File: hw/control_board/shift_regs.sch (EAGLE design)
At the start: 137 parts, among them IC1 74HC595D, IC13 STM32F10XCXT6, IC2 74HC595D, IC3 74HC595D, IC4 74HC595D, IC5 74HC595D, IC6 74HC595D, IC7 74HC595D, IC8 74HC595D, IC9 ESP8266, Q1 4MHz, Q2 32768KHz, T1 BC847, T10 BC847, T11 BC847, T12 BC847, T13 BC847, T14 BC847, T15 BC847, T16 BC847, T2 BC847, T3 BC847, T4 BC847, T5 BC847, T6 BC847, T7 BC847, T8 BC847, T9 BC847

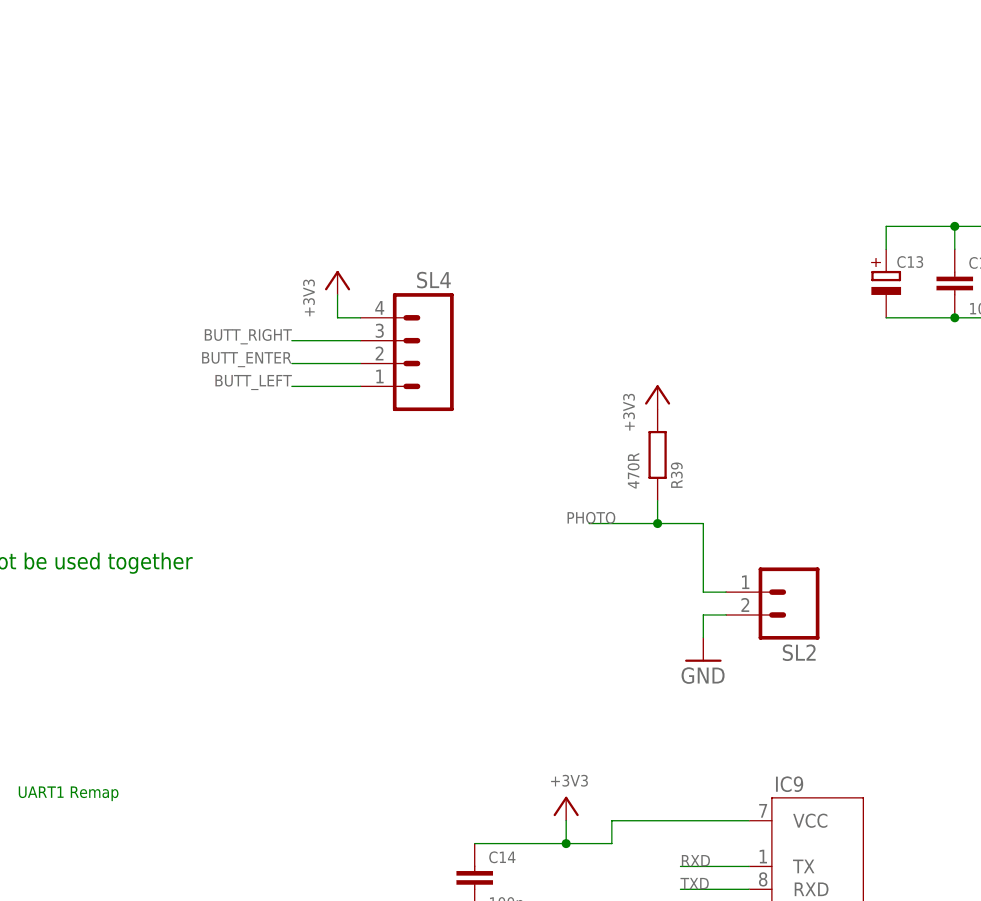
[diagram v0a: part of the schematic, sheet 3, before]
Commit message: added control buttons to the control PCB
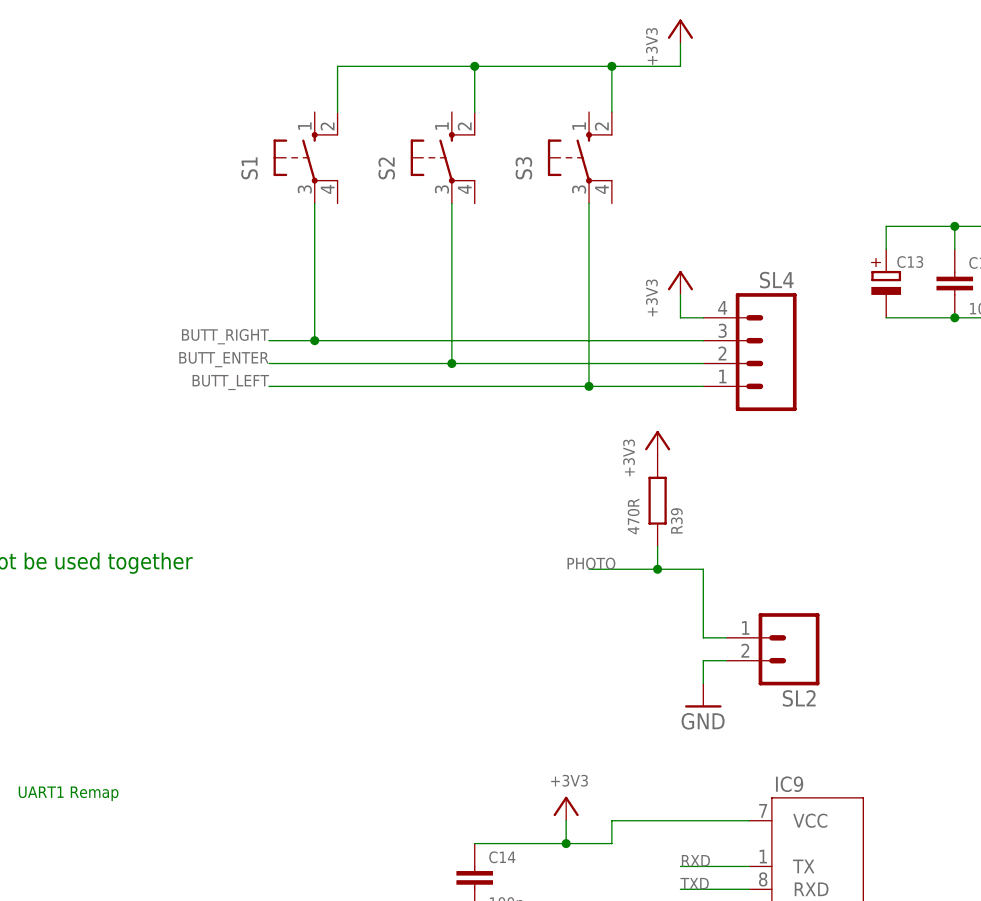
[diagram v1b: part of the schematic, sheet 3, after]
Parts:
- added S1, S2, S3: (no value), switch-omron:10-XX
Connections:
- net +3V3: now also S1.S1, S2.S1, S3.S1
- net BUTT_ENTER: now also S2.P
- net BUTT_LEFT: now also S3.P
- net BUTT_RIGHT: now also S1.P
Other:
- moved on the sheet: R39, SL2, SL4
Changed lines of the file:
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@@
 <part name="SL4" library="con-amp-quick" deviceset="M04" device=""/>
 <part name="+3V2" library="supply1" deviceset="+3V3" device=""/>
+<part name="S1" library="switch-omron" deviceset="10-XX" device=""/>
+<part name="S2" library="switch-omron" deviceset="10-XX" device=""/>
+<part name="S3" library="switch-omron" deviceset="10-XX" device=""/>
+<part name="+3V3" library="supply1" deviceset="+3V3" device=""/>
 </parts>
 <sheets>
@@
 <attribute name="VALUE" x="118.364" y="33.401" size="1.27" layer="96" font="vector"/>
 </instance>
-<instance part="R39" gate="G$1" x="137.16" y="121.92" smashed="yes" rot="MR90">
-<attribute name="NAME" x="138.6586" y="118.11" size="1.27" layer="95" font="vector" rot="MR90"/>
-<attribute name="VALUE" x="133.858" y="118.11" size="1.27" layer="96" font="vector" rot="MR90"/>
+<instance part="R39" gate="G$1" x="137.16" y="116.84" smashed="yes" rot="MR90">
+<attribute name="NAME" x="138.6586" y="113.03" size="1.27" layer="95" font="vector" rot="MR90"/>
+<attribute name="VALUE" x="133.858" y="113.03" size="1.27" layer="96" font="vector" rot="MR90"/>
 </instance>
-<instance part="+3V1" gate="G$1" x="137.16" y="129.54" smashed="yes">
-<attribute name="VALUE" x="134.62" y="124.46" size="1.27" layer="96" font="vector" rot="R90"/>
+<instance part="+3V1" gate="G$1" x="137.16" y="124.46" smashed="yes">
+<attribute name="VALUE" x="134.62" y="119.38" size="1.27" layer="96" font="vector" rot="R90"/>
 </instance>
 <instance part="SL3" gate="G$1" x="101.6" y="33.02" smashed="yes">
@@
 <attribute name="VALUE" x="241.3" y="101.6" size="1.27" layer="96" font="vector" rot="R90"/>
 </instance>
-<instance part="SL2" gate="G$1" x="152.4" y="106.68" rot="R180"/>
-<instance part="GND21" gate="1" x="142.24" y="99.06"/>
+<instance part="SL2" gate="G$1" x="152.4" y="101.6" rot="R180"/>
+<instance part="GND21" gate="1" x="142.24" y="93.98"/>
 <instance part="IC9" gate="G$1" x="154.94" y="73.66"/>
-<instance part="SL4" gate="G$1" x="109.22" y="132.08" rot="MR0"/>
-<instance part="+3V2" gate="G$1" x="101.6" y="142.24" smashed="yes">
-<attribute name="VALUE" x="99.06" y="137.16" size="1.27" layer="96" font="vector" rot="R90"/>
+<instance part="SL4" gate="G$1" x="147.32" y="132.08" rot="MR0"/>
+<instance part="+3V2" gate="G$1" x="139.7" y="142.24" smashed="yes">
+<attribute name="VALUE" x="137.16" y="137.16" size="1.27" layer="96" font="vector" rot="R90"/>
+</instance>
+<instance part="S1" gate="1" x="99.06" y="154.94"/>
+<instance part="S2" gate="1" x="114.3" y="154.94"/>
+<instance part="S3" gate="1" x="129.54" y="154.94"/>
+<instance part="+3V3" gate="G$1" x="139.7" y="170.18" smashed="yes">
+<attribute name="VALUE" x="137.16" y="165.1" size="1.27" layer="96" font="vector" rot="R90"/>
 </instance>
 </instances>
@@
 </segment>
 <segment>
-<wire x1="142.24" y1="101.6" x2="142.24" y2="104.14" width="0.1524" layer="91"/>
-<wire x1="142.24" y1="104.14" x2="144.78" y2="104.14" width="0.1524" layer="91"/>
+<wire x1="142.24" y1="96.52" x2="142.24" y2="99.06" width="0.1524" layer="91"/>
+<wire x1="142.24" y1="99.06" x2="144.78" y2="99.06" width="0.1524" layer="91"/>
 <pinref part="GND21" gate="1" pin="GND"/>
 <pinref part="SL2" gate="G$1" pin="2"/>
@@
 <pinref part="+3V2" gate="G$1" pin="+3V3"/>
 <pinref part="SL4" gate="G$1" pin="4"/>
-<wire x1="101.6" y1="139.7" x2="101.6" y2="137.16" width="0.1524" layer="91"/>
-<wire x1="101.6" y1="137.16" x2="104.14" y2="137.16" width="0.1524" layer="91"/>
+<wire x1="139.7" y1="139.7" x2="139.7" y2="137.16" width="0.1524" layer="91"/>
+<wire x1="139.7" y1="137.16" x2="142.24" y2="137.16" width="0.1524" layer="91"/>
+</segment>
+<segment>
+<wire x1="101.6" y1="165.1" x2="116.84" y2="165.1" width="0.1524" layer="91"/>
+<pinref part="+3V3" gate="G$1" pin="+3V3"/>
+<wire x1="116.84" y1="165.1" x2="132.08" y2="165.1" width="0.1524" layer="91"/>
+<wire x1="132.08" y1="165.1" x2="139.7" y2="165.1" width="0.1524" layer="91"/>
+<wire x1="139.7" y1="165.1" x2="139.7" y2="167.64" width="0.1524" layer="91"/>
+<pinref part="S3" gate="1" pin="S1"/>
+<wire x1="132.08" y1="160.02" x2="132.08" y2="165.1" width="0.1524" layer="91"/>
+<junction x="132.08" y="165.1"/>
+<pinref part="S2" gate="1" pin="S1"/>
+<wire x1="116.84" y1="160.02" x2="116.84" y2="165.1" width="0.1524" layer="91"/>
+<junction x="116.84" y="165.1"/>
+<pinref part="S1" gate="1" pin="S1"/>
+<wire x1="101.6" y1="160.02" x2="101.6" y2="165.1" width="0.1524" layer="91"/>
 </segment>
 </net>
@@
 <segment>
 <pinref part="SL4" gate="G$1" pin="1"/>
-<wire x1="104.14" y1="129.54" x2="96.52" y2="129.54" width="0.1524" layer="91"/>
-<label x="96.52" y="129.54" size="1.27" layer="95" font="vector" rot="MR0"/>
+<wire x1="142.24" y1="129.54" x2="129.54" y2="129.54" width="0.1524" layer="91"/>
+<label x="93.98" y="129.54" size="1.27" layer="95" font="vector" rot="MR0"/>
+<pinref part="S3" gate="1" pin="P"/>
+<wire x1="129.54" y1="129.54" x2="93.98" y2="129.54" width="0.1524" layer="91"/>
+<wire x1="129.54" y1="149.86" x2="129.54" y2="129.54" width="0.1524" layer="91"/>
+<junction x="129.54" y="129.54"/>
 </segment>
 </net>
@@
 <net name="PHOTO" class="0">
 <segment>
-<wire x1="142.24" y1="114.3" x2="137.16" y2="114.3" width="0.1524" layer="91"/>
-<wire x1="137.16" y1="114.3" x2="129.54" y2="114.3" width="0.1524" layer="91"/>
-<wire x1="137.16" y1="116.84" x2="137.16" y2="114.3" width="0.1524" layer="91"/>
-<wire x1="144.78" y1="106.68" x2="142.24" y2="106.68" width="0.1524" layer="91"/>
-<wire x1="142.24" y1="106.68" x2="142.24" y2="114.3" width="0.1524" layer="91"/>
-<junction x="137.16" y="114.3"/>
-<label x="127" y="114.3" size="1.27" layer="95" font="vector"/>
+<wire x1="142.24" y1="109.22" x2="137.16" y2="109.22" width="0.1524" layer="91"/>
+<wire x1="137.16" y1="109.22" x2="129.54" y2="109.22" width="0.1524" layer="91"/>
+<wire x1="137.16" y1="111.76" x2="137.16" y2="109.22" width="0.1524" layer="91"/>
+<wire x1="144.78" y1="101.6" x2="142.24" y2="101.6" width="0.1524" layer="91"/>
+<wire x1="142.24" y1="101.6" x2="142.24" y2="109.22" width="0.1524" layer="91"/>
+<junction x="137.16" y="109.22"/>
+<label x="127" y="109.22" size="1.27" layer="95" font="vector"/>
 <pinref part="R39" gate="G$1" pin="1"/>
 <pinref part="SL2" gate="G$1" pin="1"/>
@@
 <segment>
 <pinref part="SL4" gate="G$1" pin="2"/>
-<wire x1="104.14" y1="132.08" x2="96.52" y2="132.08" width="0.1524" layer="91"/>
-<label x="96.52" y="132.08" size="1.27" layer="95" font="vector" rot="MR0"/>
+<wire x1="142.24" y1="132.08" x2="114.3" y2="132.08" width="0.1524" layer="91"/>
+<label x="93.98" y="132.08" size="1.27" layer="95" font="vector" rot="MR0"/>
+<pinref part="S2" gate="1" pin="P"/>
+<wire x1="114.3" y1="132.08" x2="93.98" y2="132.08" width="0.1524" layer="91"/>
+<wire x1="114.3" y1="149.86" x2="114.3" y2="132.08" width="0.1524" layer="91"/>
+<junction x="114.3" y="132.08"/>
 </segment>
 </net>
@@
 <segment>
 <pinref part="SL4" gate="G$1" pin="3"/>
-<wire x1="104.14" y1="134.62" x2="96.52" y2="134.62" width="0.1524" layer="91"/>
-<label x="96.52" y="134.62" size="1.27" layer="95" font="vector" rot="MR0"/>
+<wire x1="142.24" y1="134.62" x2="99.06" y2="134.62" width="0.1524" layer="91"/>
+<label x="93.98" y="134.62" size="1.27" layer="95" font="vector" rot="MR0"/>
+<pinref part="S1" gate="1" pin="P"/>
+<wire x1="99.06" y1="134.62" x2="93.98" y2="134.62" width="0.1524" layer="91"/>
+<wire x1="99.06" y1="149.86" x2="99.06" y2="134.62" width="0.1524" layer="91"/>
+<junction x="99.06" y="134.62"/>
 </segment>
 </net>
